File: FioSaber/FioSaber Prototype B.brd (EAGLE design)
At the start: 26.7 x 44.7 mm, 17 parts, among them P1 WIICHUCK, T1 2N2222

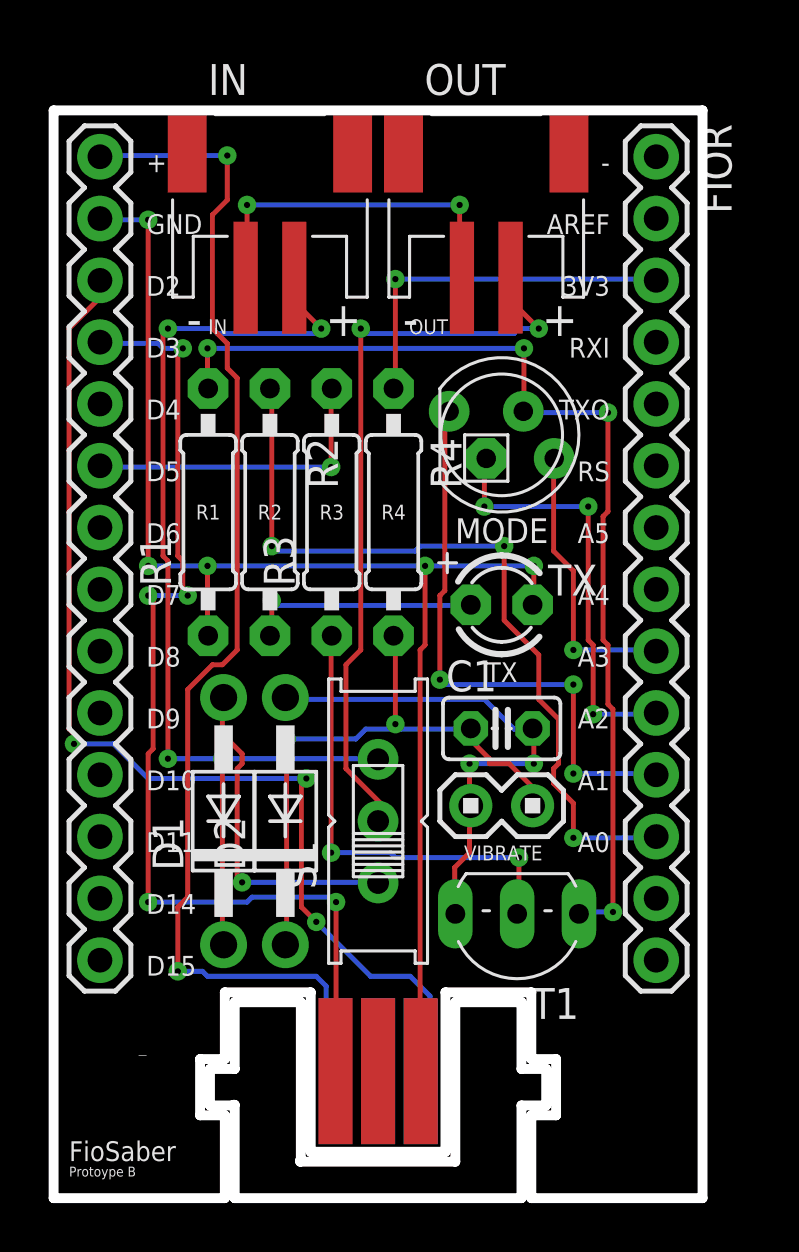
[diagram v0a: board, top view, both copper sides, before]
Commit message: added manual mode switch
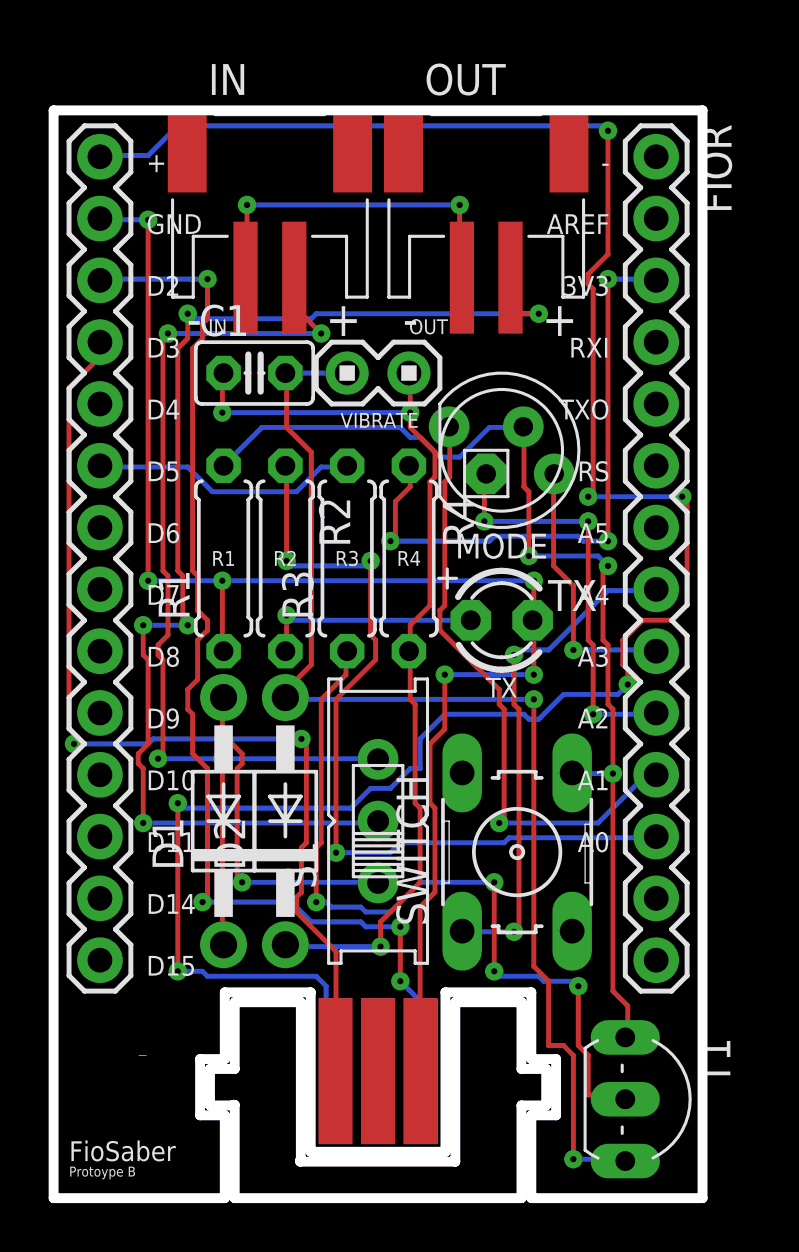
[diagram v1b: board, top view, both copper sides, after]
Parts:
- added SWITCH: (no value), switch-omron:B3F-10XX
- R1, R2, R3, R4: device adafruit:0207/10 -> adafruit:0207/7
- moved U$2 18.5 mm to (11.4, 35.6)
- moved C1 17.8 mm to (7.62, 35.6)
- moved T1 8.54 mm to (24.1, 5.71), turned to 270 degrees
- moved R1 2.01 mm to (6.35, 27.9)
- moved R2 2.01 mm to (8.89, 27.9)
- moved R3 2.01 mm to (11.4, 27.9)
- moved R4 2.01 mm to (14.0, 27.9)
- moved MODE 0.64 mm to (17.8, 32.4)
- moved TX 0.64 mm to (17.8, 25.4)
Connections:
- new net N$14: FIOR.8, SWITCH.1
- net N$13: now also SWITCH.4
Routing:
- net N$1: track 50.8 -> 89.2 mm, vias 2 -> 6
- net N$19: track 21.3 -> 49.1 mm
- net N$14: track 0.00 -> 20.6 mm, vias 0 -> 2
- net N$10: track 31.2 -> 50.4 mm, vias 2 -> 5
- net N$20: track 24.9 -> 38.7 mm, vias 2 -> 3
- net N$18: track 19.1 -> 32.4 mm, vias 2 -> 4
- net N$12: track 15.3 -> 25.3 mm, vias 1 -> 3
- net N$9: track 57.4 -> 60.0 mm, vias 5 -> 6
- net N$4: track 43.1 -> 41.1 mm, vias 5 -> 2
- net N$16: track 12.7 -> 11.0 mm, vias 1 -> 0
- net N$13: track 43.0 -> 44.4 mm, vias 4 -> 3
- net N$6: track 23.9 -> 24.9 mm, vias 3 -> 1
- net N$3: track 45.3 -> 46.1 mm, vias 3 -> 4
- net N$17: track 33.0 -> 33.7 mm
- net N$8: track 11.6 -> 11.0 mm
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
